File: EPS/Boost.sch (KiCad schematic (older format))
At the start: 45 parts

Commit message: Finalized SCH (beta version) and started pcb
Capacitor banks might need to be reassigned to other locations.
No RBF pin on this SCH or PCB.
Battery gound deployment switch is fully mechanical (no mosfet switch on low side).
PCB of the prototype started. Main power converters and current measuring devices layed out.
SCH still requires ESD protection diodes!
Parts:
- removed C? (x3): CP, symbol CP
- C26, C27, C28, C29, C30, C31, C35, C36, C37: renamed from C?; footprint (none) -> Capacitors_SMD:C_0603
- C32, C33, C34, C38, C39, C40: renamed from C?; footprint (none) -> Capacitors_Tantalum_SMD:CP_Tantalum_Case-C_EIA-6032-28_Reflow
- D1, D2, D3: renamed from D?; footprint (none) -> Diodes_SMD:D_SOD-123
- L2, L3, L4: renamed from L?; footprint (none) -> Inductors_THT:L_Axial_L7.0mm_D3.3mm_P5.08mm_Vertical_Fastron_MICC
- MAX1, MAX2, MAX3: renamed from MAX?; footprint (none) -> Housings_SSOP:MSOP-10_3x3mm_Pitch0.5mm
- MAX53951, MAX53952, MAX53953: renamed from MAX5395?; footprint (none) -> Housings_DFN_QFN:DFN-8_2x2mm_Pitch0.5mm
- Q1, Q2, Q3: renamed from Q?; footprint (none) -> TO_SOT_Packages_SMD:SOT-23
- R13, R14, R15, R19, R20, R21, R22, R23, R24: renamed from R?; footprint (none) -> Resistors_SMD:R_0603
- R16, R17, R18: renamed from R?; footprint (none) -> Resistors_SMD:R_0805
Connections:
- net 3V3 renamed +3V3
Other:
- note added: "Capacitor bank!"
- moved on the sheet: MAX53952, MAX53953, R23, R24

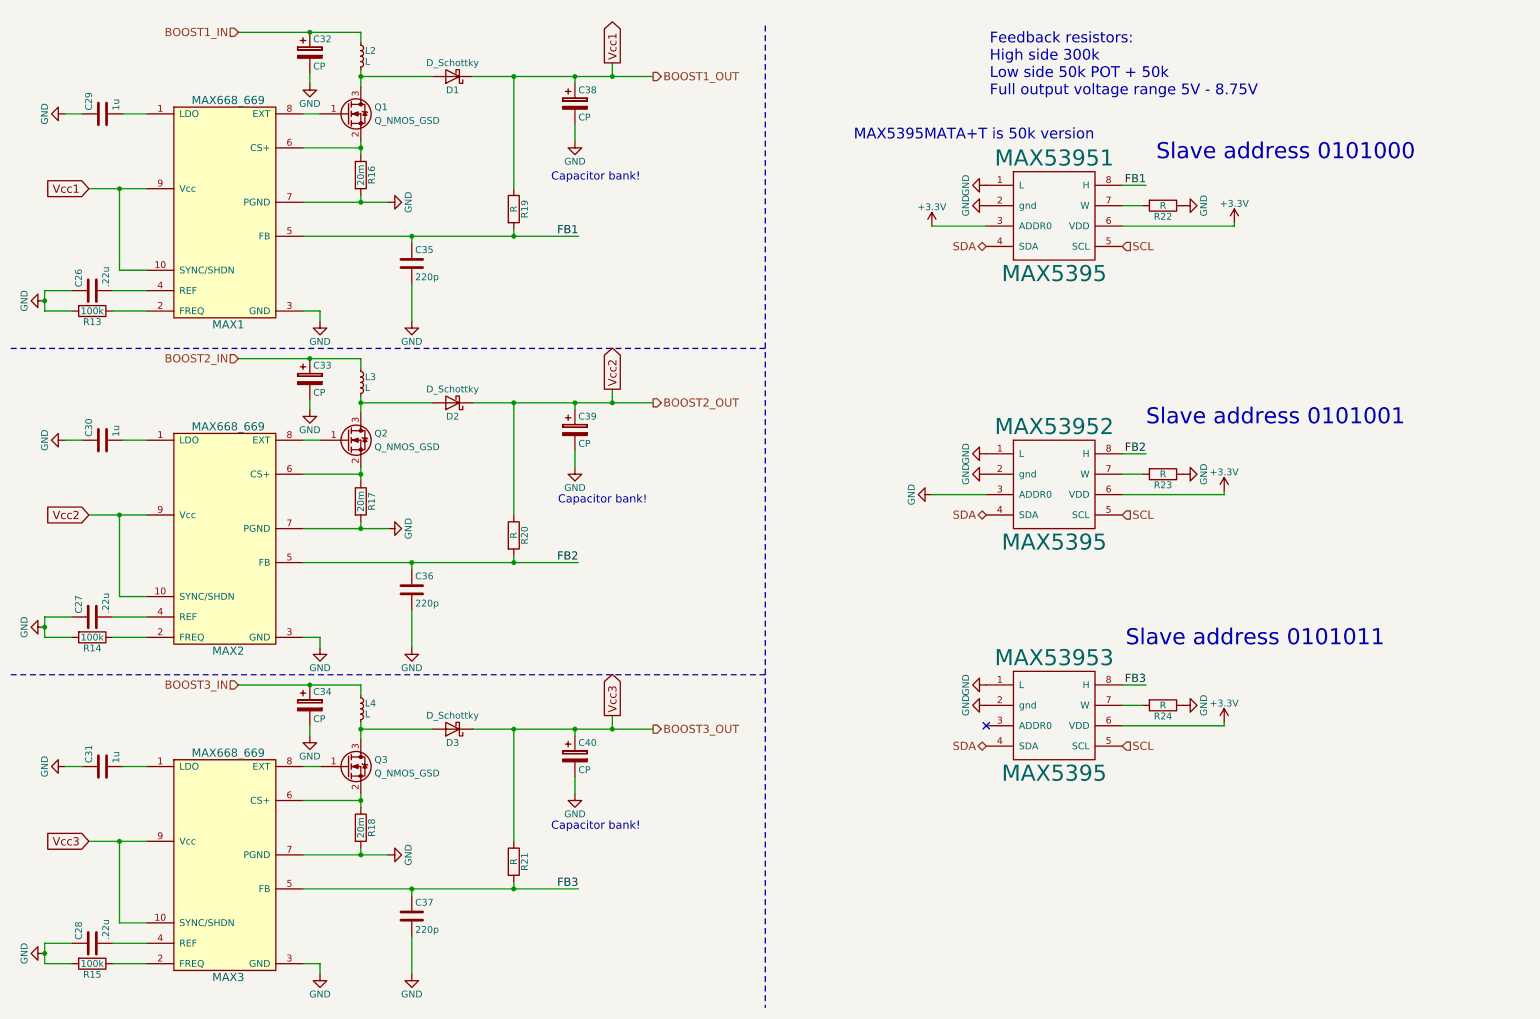
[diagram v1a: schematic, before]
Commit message: PCB updated
Added testpoints and updated PCB
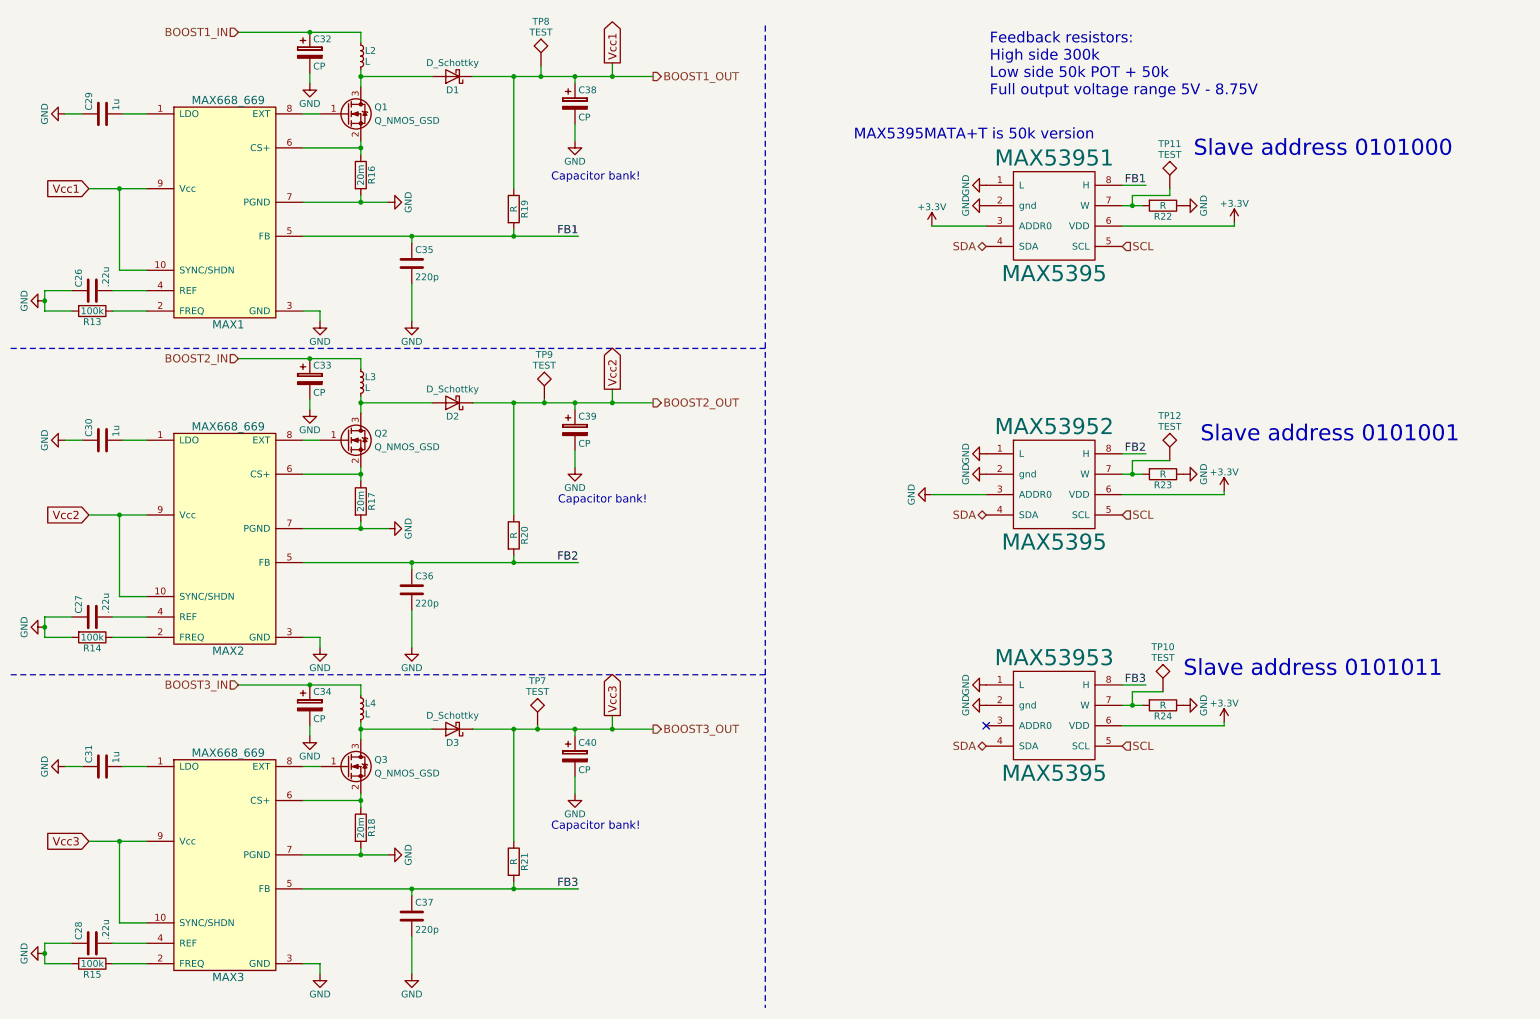
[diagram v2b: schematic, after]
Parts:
- added TP10, TP11, TP12, TP7, TP8, TP9: TEST, Measurement_Points:Measurement_Point_Round-SMD-Pad_Small, symbol TEST
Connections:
- net Vcc1: now also TP8.1
- net Vcc2: now also TP9.1
- net Vcc3: now also TP7.1
- net at MAX53951.7 (W), R22.2: now also TP11.1
- net at MAX53952.7 (W), R23.2: now also TP12.1
- net at MAX53953.7 (W), R24.2: now also TP10.1
